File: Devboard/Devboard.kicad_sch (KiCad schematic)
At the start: 36 parts, among them IC1 114993390, J1 USB_C_Receptacle_USB2.0_16P, J2 SWD, J3 RMF, SW1 SHPHLD, SW2 RST, SW3 SW_Push, U1 NPM1304-QEAA-R, U2 E73-2G4M08S1C, U3 SRV05-4, Y1 32.768

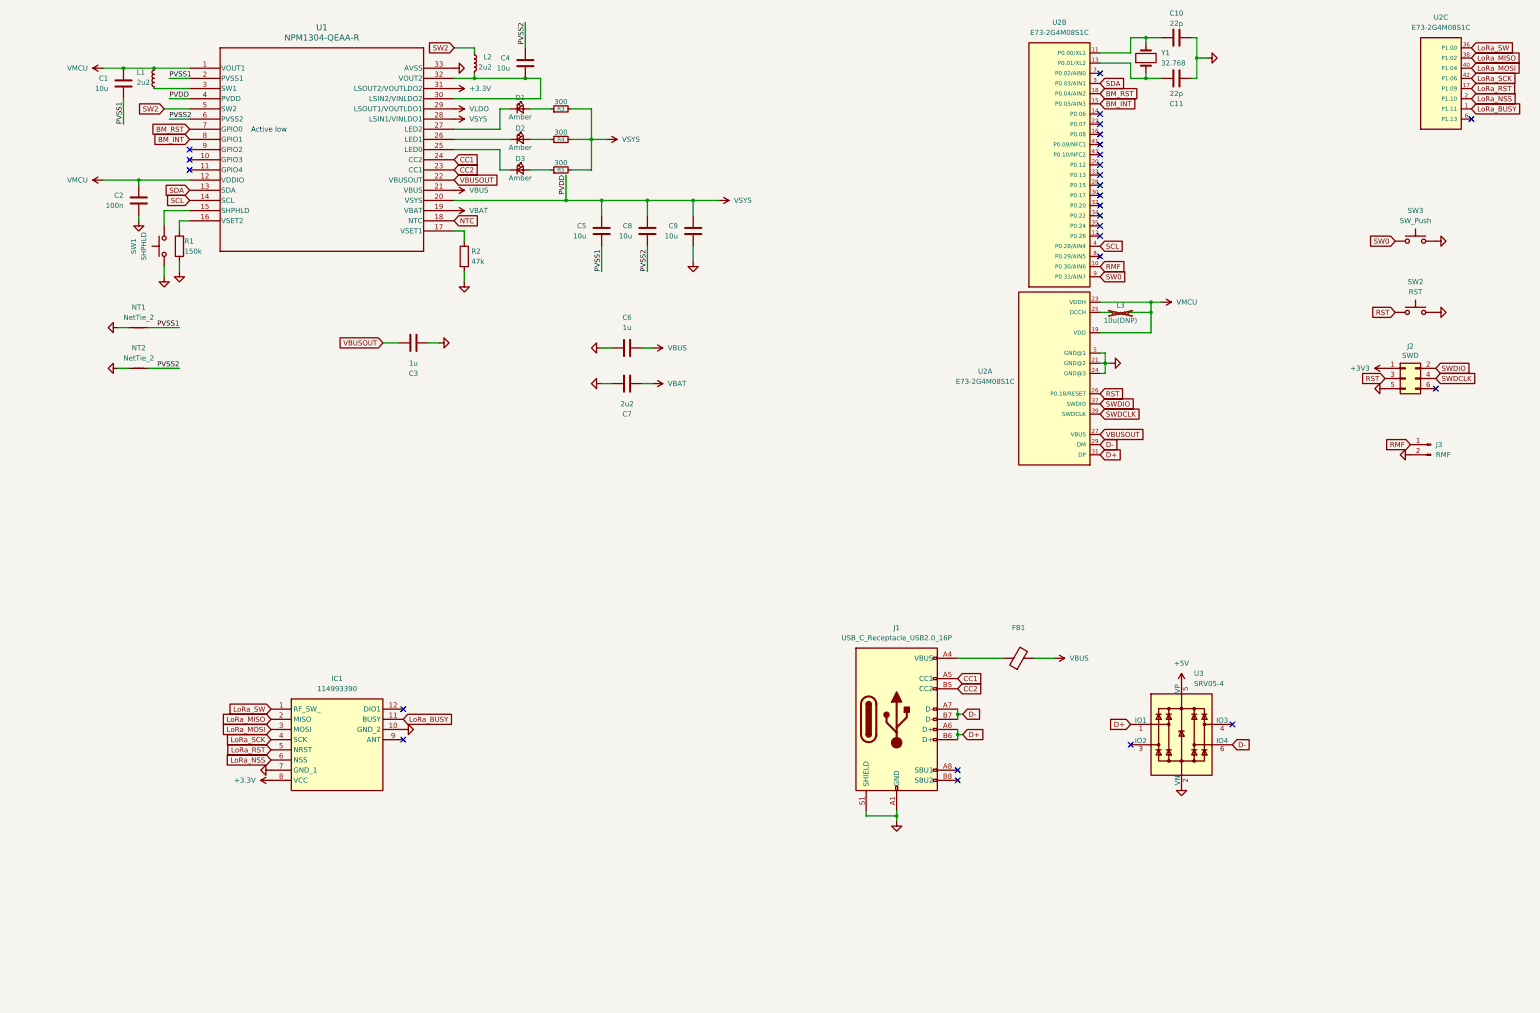
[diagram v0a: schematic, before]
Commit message: added sd card, and refined design
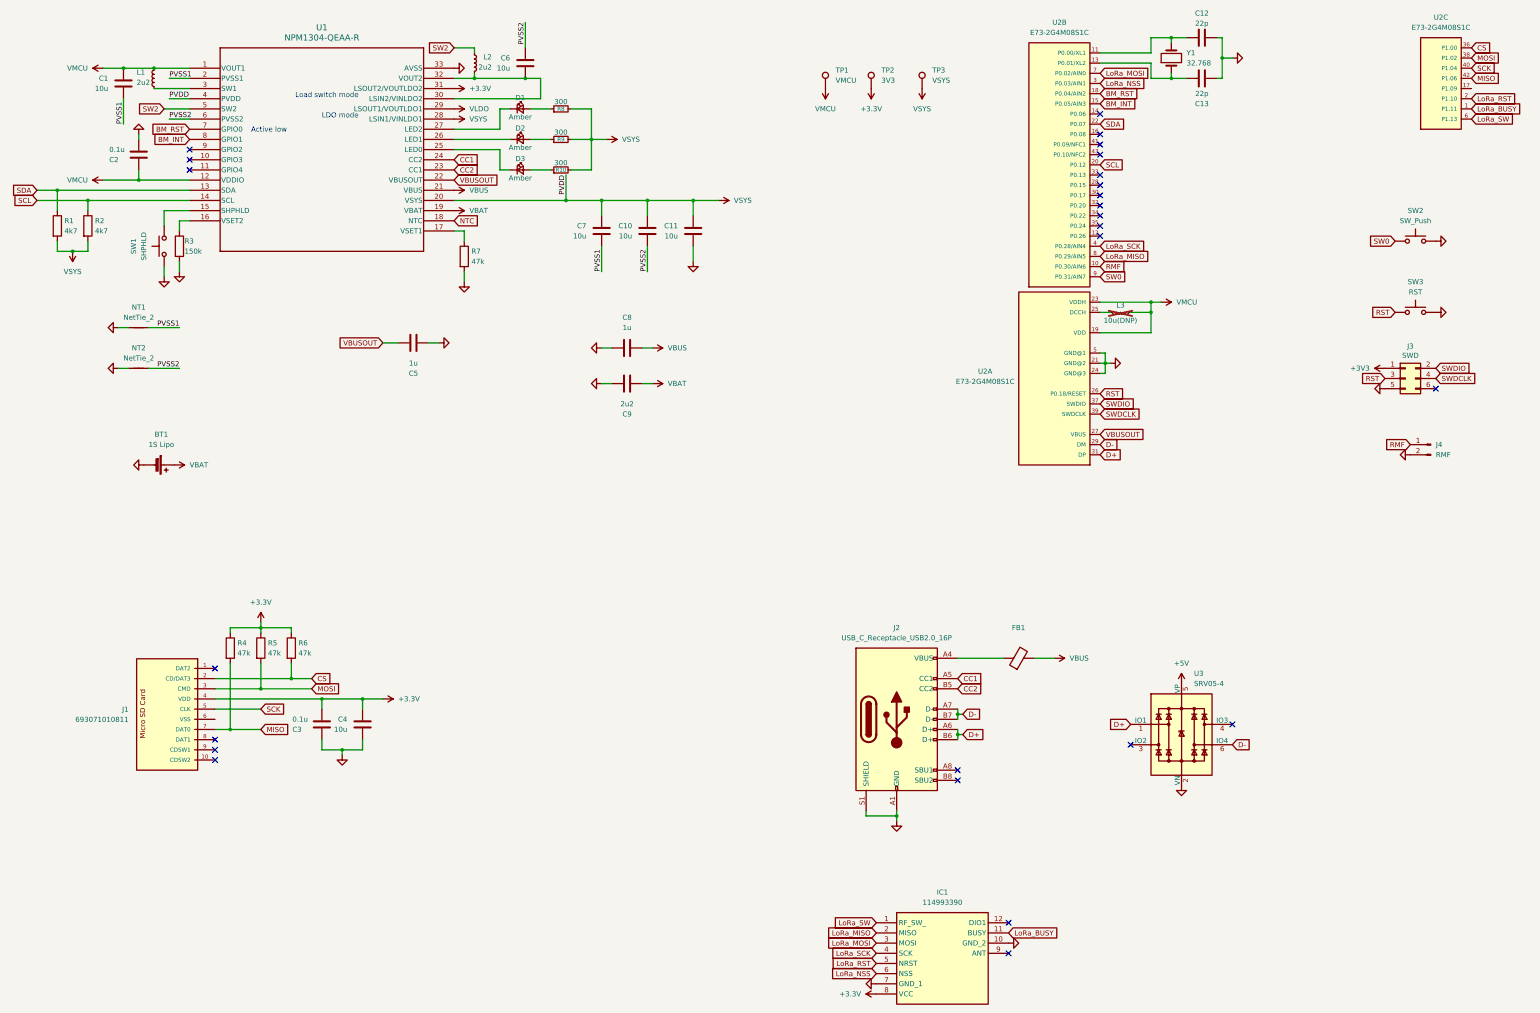
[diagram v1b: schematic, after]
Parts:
- added BT1: 1S Lipo, Connector_JST:JST_XH_B2B-XH-A_1x02_P2.50mm_Vertical, symbol Device:Battery_Cell
- added C3: 0.1u, Capacitor_SMD:C_1206_3216Metric_Pad1.33x1.80mm_HandSolder, symbol Device:C
- added C4: 10u, Capacitor_SMD:C_1206_3216Metric_Pad1.33x1.80mm_HandSolder, symbol Device:C
- added J1: 693071010811, 693071010811:693071010811, symbol 693071010811:693071010811
- added R1, R2: 4k7, Resistor_SMD:R_1206_3216Metric_Pad1.30x1.75mm_HandSolder, symbol Device:R
- added R4, R5, R6: 47k, Resistor_SMD:R_1206_3216Metric_Pad1.30x1.75mm_HandSolder, symbol Device:R
- added TP1: VMCU, TestPoint:TestPoint_Pad_D1.0mm, symbol Connector:TestPoint
- added TP2: 3V3, TestPoint:TestPoint_Pad_D1.0mm, symbol Connector:TestPoint
- added TP3: VSYS, TestPoint:TestPoint_Pad_D1.0mm, symbol Connector:TestPoint
- C2: value 100n -> 0.1u
- Y1: footprint Crystal:Crystal_SMD_MicroCrystal_CC1V-T1A-2Pin_8.0x3.7mm -> Project_Components:WE-XTAL_CFPX-217
- renumbered C8 to C10, C9 to C11, C10 to C12, C11 to C13, C3 to C5, C4 to C6, C5 to C7, C6 to C8, C7 to C9, J1 to J2, J2 to J3, J3 to J4, R5 to R10, R1 to R3, R2 to R7, R3 to R8, R4 to R9, SW3 to SW2, SW2 to SW3
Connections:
- net +3.3V: now also C3.2, C4.2, J1.4 (VDD), R4.1, R5.1, R6.1, TP2.1
- net GND: now also BT1.2 (-), C3.1, C4.1
- net LoRa_MISO: now also U2.8 (P0.29/AIN5); no longer U2.38 (P1.02)
- net LoRa_MOSI: now also U2.7 (P0.02/AIN0); no longer U2.40 (P1.04)
- net LoRa_NSS: now also U2.3 (P0.03/AIN1); no longer U2.2 (P1.10)
- net LoRa_RST: now also U2.2 (P1.10); no longer U2.17 (P1.09)
- net LoRa_SCK: now also U2.4 (P0.28/AIN4); no longer U2.42 (P1.06)
- net LoRa_SW: now also U2.6 (P1.13); no longer U2.36 (P1.00)
- net SCL: now also U2.20 (P0.12), R2.1; no longer U2.4 (P0.28/AIN4)
- net SDA: now also U2.22 (P0.07), R1.1; no longer U2.3 (P0.03/AIN1)
- net VBAT: now also BT1.1 (+)
- net VMCU: now also TP1.1
- net VSYS: now also R1.2, R2.2, TP3.1
- new net: J1.10 (CDSW2), J1.10-1 (CDSW2)
- new net: J1.9 (CDSW1), J1.9-1 (CDSW1)
- new net CS: J1.2 (CD/DAT3), R6.2, U2.36 (P1.00)
- new net MISO: J1.7 (DAT0), R4.2, U2.42 (P1.06)
- new net MOSI: J1.3 (CMD), R5.2, U2.38 (P1.02)
- new net SCK: J1.5 (CLK), U2.40 (P1.04)
- no-connect marks 26 -> 25
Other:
- note added: "LDO mode"
- note added: "Load switch mode"
- moved on the sheet: C12, C13, C2, IC1, Y1

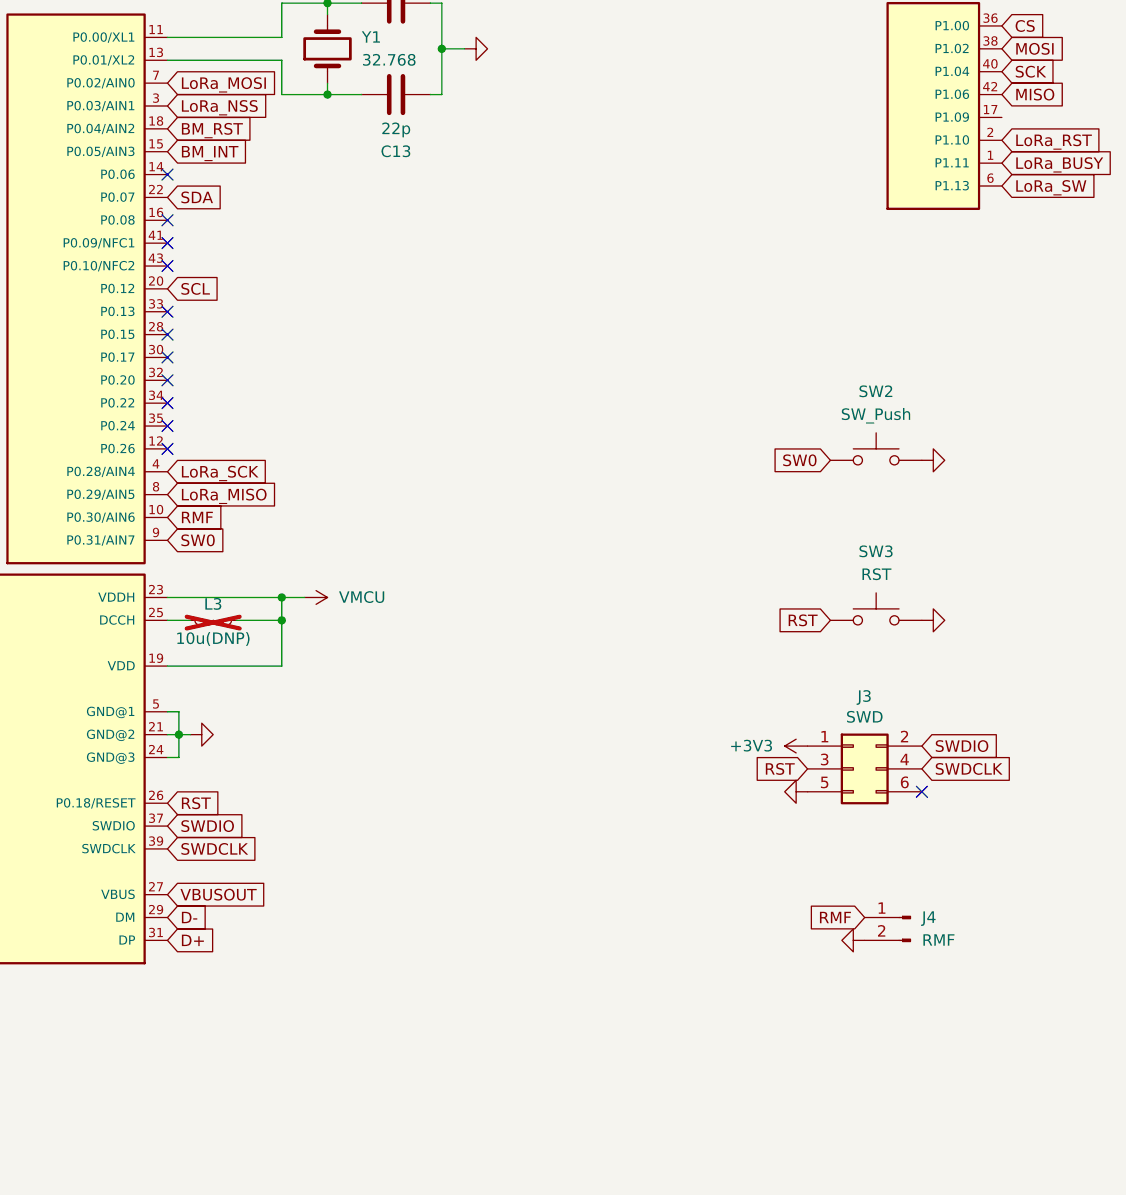
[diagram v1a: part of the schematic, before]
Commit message: Added external pin
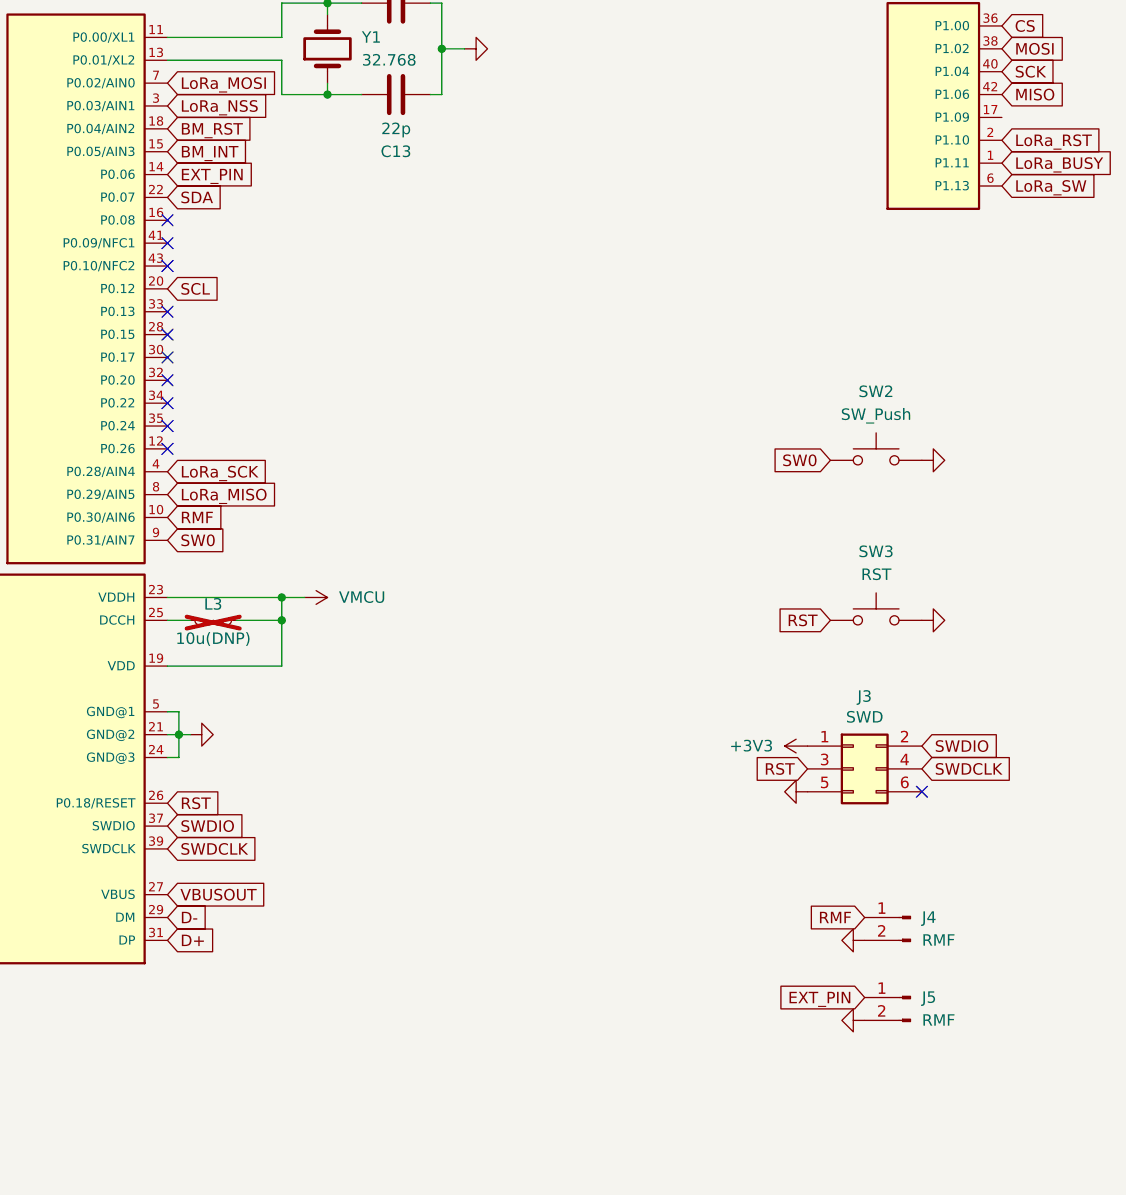
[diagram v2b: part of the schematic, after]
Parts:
- added J5: RMF, Connector_PinHeader_2.54mm:PinHeader_1x02_P2.54mm_Vertical, symbol Connector:Conn_01x02_Pin
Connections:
- net GND: now also J5.2 (Pin_2)
- net EXT_PIN: now reaches U2.14 (P0.06)
- net EXT_PIN: now also J5.1 (Pin_1)
- no-connect marks 25 -> 24
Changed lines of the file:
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@@
 	)
 	(no_connect
-		(at 294.64 48.26)
-	)
-	(no_connect
 		(at 327.66 200.66)
 	)
@@
 		)
 	)
+	(global_label "EXT_PIN"
+		(shape input)
+		(at 294.64 48.26 0)
+		(fields_autoplaced yes)
+		(effects
+			(font
+				(size 1.27 1.27)
+			)
+			(justify left)
+		)
+		(property "Intersheetrefs" "${INTERSHEET_REFS}"
+			(at 305.1242 48.26 0)
+			(hide yes)
+			(show_name no)
+			(do_not_autoplace no)
+			(effects
+				(font
+					(size 1.27 1.27)
+				)
+				(justify left)
+			)
+		)
+	)
 	(global_label "SW2"
 		(shape input)
@@
 		)
 	)
+	(global_label "EXT_PIN"
+		(shape input)
+		(at 372.11 139.7 180)
+		(fields_autoplaced yes)
+		(effects
+			(font
+				(size 1.27 1.27)
+			)
+			(justify right)
+		)
+		(property "Intersheetrefs" "${INTERSHEET_REFS}"
+			(at 361.6258 139.7 0)
+			(hide yes)
+			(show_name no)
+			(do_not_autoplace no)
+			(effects
+				(font
+					(size 1.27 1.27)
+				)
+				(justify right)
+			)
+		)
+	)
 	(global_label "RMF"
 		(shape input)
@@
 	)
 	(symbol
+		(lib_id "power:GND")
+		(at 372.11 142.24 270)
+		(unit 1)
+		(body_style 1)
+		(exclude_from_sim no)
+		(in_bom yes)
+		(on_board yes)
+		(in_pos_files yes)
+		(dnp no)
+		(property "Reference" "#PWR047"
+			(at 365.76 142.24 0)
+			(hide yes)
+			(show_name no)
+			(do_not_autoplace no)
+			(effects
+				(font
+					(size 1.27 1.27)
+				)
+			)
+		)
+		(property "Value" "GND"
+			(at 368.8588 142.367 90)
+			(hide yes)
+			(show_name no)
+			(do_not_autoplace no)
+			(effects
+				(font
+					(size 1.27 1.27)
+				)
+				(justify right)
+			)
+		)
+		(property "Footprint" ""
+			(at 372.11 142.24 0)
+			(hide yes)
+			(show_name no)
+			(do_not_autoplace no)
+			(effects
+				(font
+					(size 1.27 1.27)
+				)
+			)
+		)
+		(property "Datasheet" ""
+			(at 372.11 142.24 0)
+			(hide yes)
+			(show_name no)
+			(do_not_autoplace no)
+			(effects
+				(font
+					(size 1.27 1.27)
+				)
+			)
+		)
+		(property "Description" ""
+			(at 372.11 142.24 0)
+			(show_name no)
+			(do_not_autoplace no)
+			(effects
+				(font
+					(size 1.27 1.27)
+				)
+			)
+		)
+		(pin "1"
+		)
+		(instances
+			(project "Devboard"
+				(path "/0a0a1e18-e167-488d-99d1-7fc114522a17"
+					(reference "#PWR047")
+					(unit 1)
+				)
+			)
+		)
+	)
+	(symbol
 		(lib_id "Device:Crystal")
 		(at 312.42 34.29 90)
@@
 					(unit 1)
 				)
+			)
+		)
+	)
+	(symbol
+		(lib_id "Connector:Conn_01x02_Pin")
+		(at 377.19 139.7 0)
+		(mirror y)
+		(unit 1)
+		(body_style 1)
+		(exclude_from_sim no)
+		(in_bom yes)
+		(on_board yes)
+		(in_pos_files yes)
+		(dnp no)
+		(fields_autoplaced yes)
+		(property "Reference" "J5"
+			(at 378.46 139.6999 0)
+			(show_name no)
+			(do_not_autoplace no)
+			(effects
+				(font
+					(size 1.27 1.27)
+				)
+				(justify right)
+			)
+		)
+		(property "Value" "RMF"
+			(at 378.46 142.2399 0)
+			(show_name no)
+			(do_not_autoplace no)
+			(effects
+				(font
+					(size 1.27 1.27)
+				)
+				(justify right)
+			)
+		)
+		(property "Footprint" "Connector_PinHeader_2.54mm:PinHeader_1x02_P2.54mm_Vertical"
+			(at 377.19 139.7 0)
+			(hide yes)
+			(show_name no)
+			(do_not_autoplace no)
+			(effects
+				(font
+					(size 1.27 1.27)
+				)
+			)
+		)
+		(property "Datasheet" ""
+			(at 377.19 139.7 0)
+			(hide yes)
+			(show_name no)
+			(do_not_autoplace no)
+			(effects
+				(font
+					(size 1.27 1.27)
+				)
+			)
+		)
+		(property "Description" "Generic connector, single row, 01x02, script generated"
+			(at 377.19 139.7 0)
+			(hide yes)
+			(show_name no)
+			(do_not_autoplace no)
+			(effects
+				(font
+					(size 1.27 1.27)
+				)
+			)
+		)
+		(pin "1"
+		)
+		(pin "2"
+		)
+		(instances
+			(project "Devboard"
+				(path "/0a0a1e18-e167-488d-99d1-7fc114522a17"
+					(reference "J5")
+					(unit 1)
+				)
